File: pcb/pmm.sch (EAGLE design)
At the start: 25 parts, among them IC3 STM32F042F4, SW3 324_SW, SW4 324_SW, U2 USBC_16P, U4 XC6206_DEV

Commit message: fixed card edge connector footprint
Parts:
- JP1: device pinhead:PINHD-2X4 -> pmm:PINHEAD_PINHD-2X4
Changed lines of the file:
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@@
 <part name="R5" library="joyAnalog" deviceset="RESISTOR" device="0805-RES" value="10K"/>
 <part name="GND10" library="supply1" deviceset="GND" device=""/>
-<part name="JP1" library="pinhead" library_urn="urn:adsk.eagle:library:325" deviceset="PINHD-2X4" device="" package3d_urn="urn:adsk.eagle:package:22461/2"/>
+<part name="JP1" library="pmm" deviceset="PINHEAD_PINHD-2X4" device=""/>
 <part name="U4" library="3pos_slide_switch" deviceset="XC6206_DEV" device=""/>
 <part name="C2" library="clock" deviceset="CAP" device="0805" value="10uF"/>

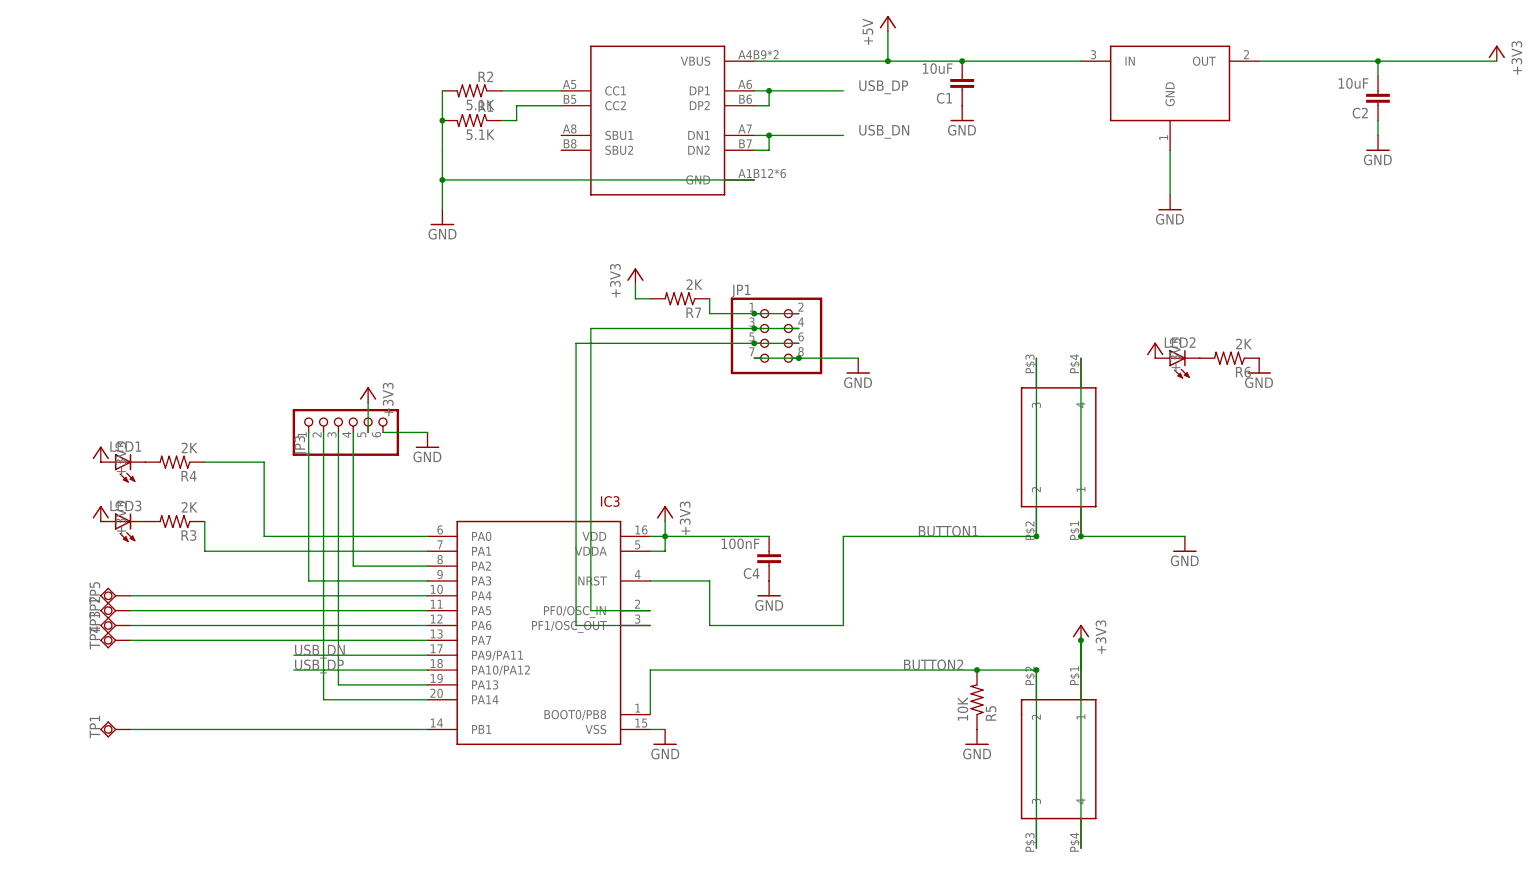
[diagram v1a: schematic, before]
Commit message: updated component values
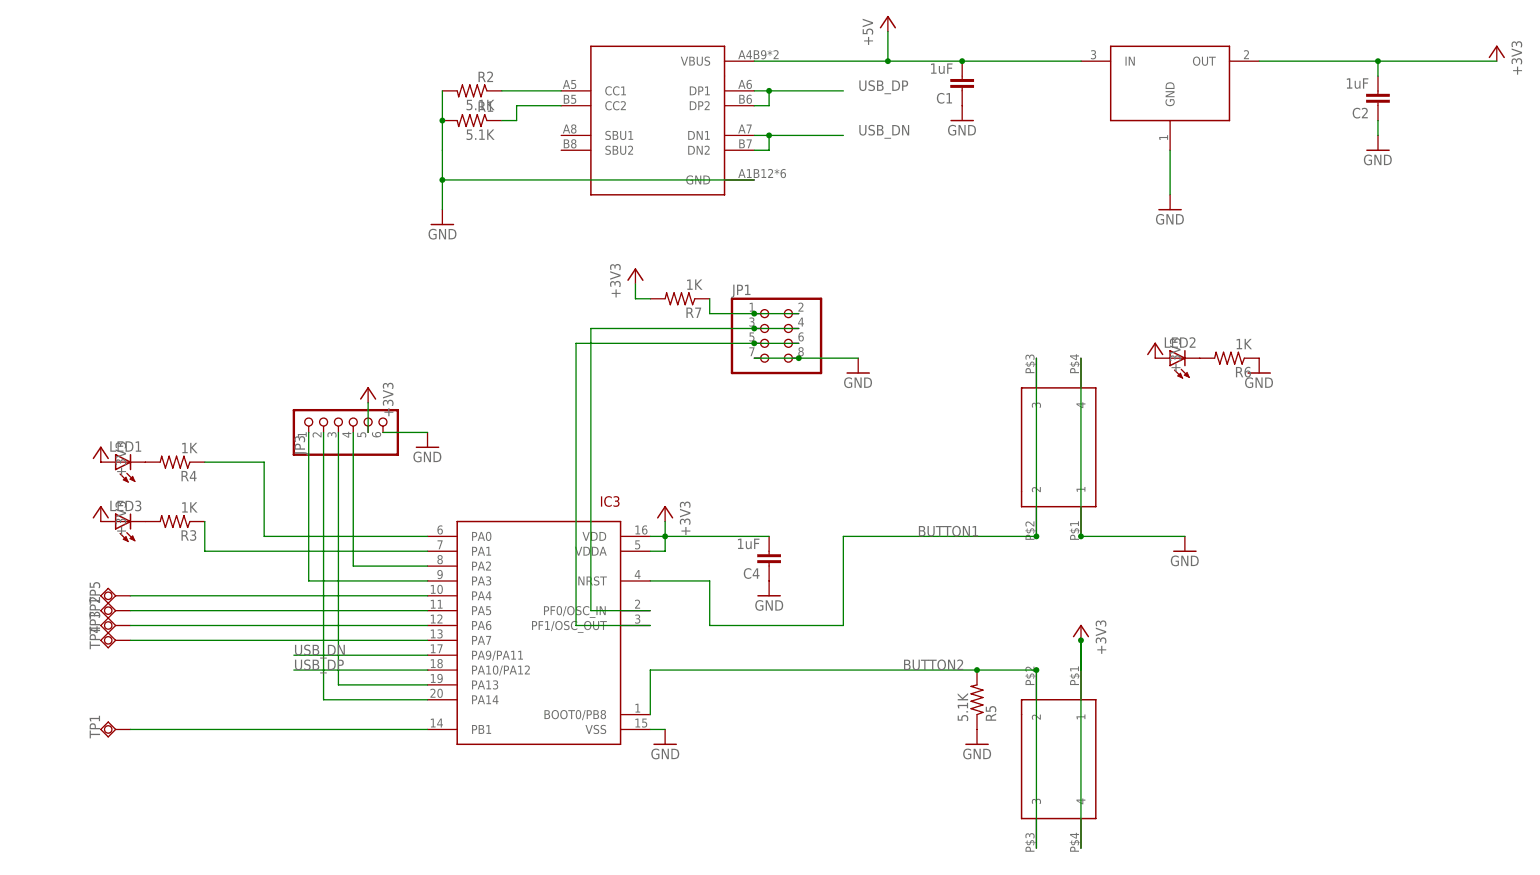
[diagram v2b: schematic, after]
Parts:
- C1, C2: value 10uF -> 1uF
- C4: value 100nF -> 1uF
- R3, R4, R6, R7: value 2K -> 1K
- R5: value 10K -> 5.1K
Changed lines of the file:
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@@
 <part name="R1" library="joyAnalog" deviceset="RESISTOR" device="0805-RES" value="5.1K"/>
 <part name="R2" library="joyAnalog" deviceset="RESISTOR" device="0805-RES" value="5.1K"/>
-<part name="C1" library="clock" deviceset="CAP" device="0805" value="10uF"/>
+<part name="C1" library="clock" deviceset="CAP" device="0805" value="1uF"/>
 <part name="GND16" library="supply1" library_urn="urn:adsk.eagle:library:371" deviceset="GND" device=""/>
 <part name="GND1" library="supply1" library_urn="urn:adsk.eagle:library:371" deviceset="GND" device=""/>
@@
 <part name="+3V1" library="supply1" library_urn="urn:adsk.eagle:library:371" deviceset="+3V3" device=""/>
 <part name="GND5" library="supply1" deviceset="GND" device=""/>
-<part name="C4" library="clock" deviceset="CAP" device="0805" value="100nF"/>
+<part name="C4" library="clock" deviceset="CAP" device="0805" value="1uF"/>
 <part name="GND8" library="supply1" deviceset="GND" device=""/>
 <part name="GND11" library="supply1" library_urn="urn:adsk.eagle:library:371" deviceset="GND" device=""/>
@@
 <part name="SW4" library="3pos_slide_switch_centered" deviceset="324_SW" device="" value="324_SW"/>
 <part name="LED1" library="adafruit" deviceset="LED" device="CHIP-LED0805"/>
-<part name="R4" library="SparkFun-Passives" deviceset="RESISTOR" device="0805-RES" value="2K"/>
+<part name="R4" library="SparkFun-Passives" deviceset="RESISTOR" device="0805-RES" value="1K"/>
 <part name="+3V9" library="backplane" deviceset="+3V3" device=""/>
 <part name="+3V16" library="backplane" deviceset="+3V3" device=""/>
 <part name="LED2" library="adafruit" deviceset="LED" device="CHIP-LED0805"/>
-<part name="R6" library="SparkFun-Passives" deviceset="RESISTOR" device="0805-RES" value="2K"/>
+<part name="R6" library="SparkFun-Passives" deviceset="RESISTOR" device="0805-RES" value="1K"/>
 <part name="GND9" library="backplane" deviceset="GND" device=""/>
 <part name="+3V2" library="supply1" library_urn="urn:adsk.eagle:library:371" deviceset="+3V3" device=""/>
-<part name="R5" library="joyAnalog" deviceset="RESISTOR" device="0805-RES" value="10K"/>
+<part name="R5" library="joyAnalog" deviceset="RESISTOR" device="0805-RES" value="5.1K"/>
 <part name="GND10" library="supply1" deviceset="GND" device=""/>
 <part name="JP1" library="pmm" deviceset="PINHEAD_PINHD-2X4" device=""/>
 <part name="U4" library="3pos_slide_switch" deviceset="XC6206_DEV" device=""/>
-<part name="C2" library="clock" deviceset="CAP" device="0805" value="10uF"/>
+<part name="C2" library="clock" deviceset="CAP" device="0805" value="1uF"/>
 <part name="GND2" library="backplane" deviceset="GND" device=""/>
 <part name="+3V3" library="backplane" deviceset="+3V3" device=""/>
 <part name="LED3" library="adafruit" deviceset="LED" device="CHIP-LED0805"/>
-<part name="R3" library="SparkFun-Passives" deviceset="RESISTOR" device="0805-RES" value="2K"/>
+<part name="R3" library="SparkFun-Passives" deviceset="RESISTOR" device="0805-RES" value="1K"/>
 <part name="+3V4" library="backplane" deviceset="+3V3" device=""/>
 <part name="JP3" library="pinhead" library_urn="urn:adsk.eagle:library:325" deviceset="PINHD-1X6" device="" package3d_urn="urn:adsk.eagle:package:22472/2"/>
 <part name="+3V6" library="supply1" library_urn="urn:adsk.eagle:library:371" deviceset="+3V3" device=""/>
 <part name="GND3" library="backplane" deviceset="GND" device=""/>
-<part name="R7" library="SparkFun-Passives" deviceset="RESISTOR" device="0805-RES" value="2K"/>
+<part name="R7" library="SparkFun-Passives" deviceset="RESISTOR" device="0805-RES" value="1K"/>
 <part name="TP1" library="testpad" library_urn="urn:adsk.eagle:library:385" deviceset="TPSQ" device="TP10SQ" package3d_urn="urn:adsk.eagle:package:27962/1" value="TPSQTP10SQ"/>
 <part name="TP2" library="testpad" library_urn="urn:adsk.eagle:library:385" deviceset="TPSQ" device="TP10SQ" package3d_urn="urn:adsk.eagle:package:27962/1" value="TPSQTP10SQ"/>

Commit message: updated pcb for next production run
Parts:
- removed SW3: 324_SW, 3pos_slide_switch_centered:324_SW
- removed TP1, TP2, TP3, TP4, TP5: TPSQTP10SQ, testpad:TPSQTP10SQ
- added JP2: (no value), pinhead:PINHD-2X3
- added U$1: PINHD1X2, adafruit_changed:PINHD1X2
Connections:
- removed net BUTTON1: IC3.NRST, SW3.2, SW3.3
- new net N$16: IC3.PA4, U$1.1
- net GND: now also JP2.1; no longer SW3.1, SW3.4
- net N$11: now also IC3.PA5, JP2.4; no longer IC3.PA7, TP4.TP
- net N$12: now also JP2.6; no longer TP3.TP
- net N$13: now also IC3.PA7, JP2.3; no longer IC3.PA5, TP2.TP
- net N$14: now also JP2.5; no longer TP1.TP
- net N$15: now also IC3.NRST, JP2.2; no longer IC3.PA4, TP5.TP
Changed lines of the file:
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@@
 <?xml version="1.0" encoding="utf-8"?>
 <!DOCTYPE eagle SYSTEM "eagle.dtd">
-<eagle version="9.6.1">
+<eagle version="9.6.2">
 <drawing>
 <settings>
@@
 <part name="GND8" library="supply1" deviceset="GND" device=""/>
 <part name="GND11" library="supply1" library_urn="urn:adsk.eagle:library:371" deviceset="GND" device=""/>
-<part name="SW3" library="3pos_slide_switch_centered" deviceset="324_SW" device="" value="324_SW"/>
 <part name="SW4" library="3pos_slide_switch_centered" deviceset="324_SW" device="" value="324_SW"/>
 <part name="LED1" library="adafruit" deviceset="LED" device="CHIP-LED0805"/>
@@
 <part name="GND3" library="backplane" deviceset="GND" device=""/>
 <part name="R7" library="SparkFun-Passives" deviceset="RESISTOR" device="0805-RES" value="1K"/>
-<part name="TP1" library="testpad" library_urn="urn:adsk.eagle:library:385" deviceset="TPSQ" device="TP10SQ" package3d_urn="urn:adsk.eagle:package:27962/1" value="TPSQTP10SQ"/>
-<part name="TP2" library="testpad" library_urn="urn:adsk.eagle:library:385" deviceset="TPSQ" device="TP10SQ" package3d_urn="urn:adsk.eagle:package:27962/1" value="TPSQTP10SQ"/>
-<part name="TP3" library="testpad" library_urn="urn:adsk.eagle:library:385" deviceset="TPSQ" device="TP10SQ" package3d_urn="urn:adsk.eagle:package:27962/1" value="TPSQTP10SQ"/>
-<part name="TP4" library="testpad" library_urn="urn:adsk.eagle:library:385" deviceset="TPSQ" device="TP10SQ" package3d_urn="urn:adsk.eagle:package:27962/1" value="TPSQTP10SQ"/>
-<part name="TP5" library="testpad" library_urn="urn:adsk.eagle:library:385" deviceset="TPSQ" device="TP10SQ" package3d_urn="urn:adsk.eagle:package:27962/1" value="TPSQTP10SQ"/>
+<part name="JP2" library="pinhead" library_urn="urn:adsk.eagle:library:325" deviceset="PINHD-2X3" device="" package3d_urn="urn:adsk.eagle:package:22462/2"/>
+<part name="U$1" library="adafruit_changed" deviceset="PINHD1X2" device=""/>
 </parts>
 <sheets>
@@
 <attribute name="VALUE" x="43.18" y="27.94" size="1.778" layer="96" rot="MR0"/>
 </instance>
-<instance part="GND11" gate="1" x="111.76" y="38.1" smashed="yes">
-<attribute name="VALUE" x="109.22" y="35.56" size="1.778" layer="96"/>
-</instance>
-<instance part="SW3" gate="G$1" x="91.44" y="55.88" smashed="yes" rot="R90"/>
+<instance part="GND11" gate="1" x="-86.36" y="-2.54" smashed="yes">
+<attribute name="VALUE" x="-88.9" y="-5.08" size="1.778" layer="96"/>
+</instance>
 <instance part="SW4" gate="G$1" x="91.44" y="2.54" smashed="yes" rot="MR270"/>
 <instance part="LED1" gate="G$1" x="-71.12" y="53.34" smashed="yes" rot="R90">
@@
 <attribute name="VALUE" x="29.21" y="84.582" size="1.778" layer="96" rot="R180"/>
 </instance>
-<instance part="TP1" gate="G$1" x="-71.12" y="7.62" smashed="yes" rot="R270">
-<attribute name="NAME" x="-75.565" y="10.16" size="1.778" layer="95" rot="R270"/>
-<attribute name="TP_SIGNAL_NAME" x="-72.39" y="5.08" size="1.778" layer="97" rot="R270"/>
-</instance>
-<instance part="TP2" gate="G$1" x="-71.12" y="27.94" smashed="yes" rot="R270">
-<attribute name="NAME" x="-75.565" y="30.48" size="1.778" layer="95" rot="R270"/>
-<attribute name="TP_SIGNAL_NAME" x="-72.39" y="25.4" size="1.778" layer="97" rot="R270"/>
-</instance>
-<instance part="TP3" gate="G$1" x="-71.12" y="25.4" smashed="yes" rot="R270">
-<attribute name="NAME" x="-75.565" y="27.94" size="1.778" layer="95" rot="R270"/>
-<attribute name="TP_SIGNAL_NAME" x="-72.39" y="22.86" size="1.778" layer="97" rot="R270"/>
-</instance>
-<instance part="TP4" gate="G$1" x="-71.12" y="22.86" smashed="yes" rot="R270">
-<attribute name="NAME" x="-75.565" y="25.4" size="1.778" layer="95" rot="R270"/>
-<attribute name="TP_SIGNAL_NAME" x="-72.39" y="20.32" size="1.778" layer="97" rot="R270"/>
-</instance>
-<instance part="TP5" gate="G$1" x="-71.12" y="30.48" smashed="yes" rot="R270">
-<attribute name="NAME" x="-75.565" y="33.02" size="1.778" layer="95" rot="R270"/>
-<attribute name="TP_SIGNAL_NAME" x="-72.39" y="27.94" size="1.778" layer="97" rot="R270"/>
+<instance part="JP2" gate="A" x="-68.58" y="-2.54" smashed="yes">
+<attribute name="NAME" x="-74.93" y="3.175" size="1.778" layer="95"/>
+<attribute name="VALUE" x="-74.93" y="-10.16" size="1.778" layer="96"/>
+</instance>
+<instance part="U$1" gate="1" x="-76.2" y="33.02" smashed="yes" rot="R180">
+<attribute name="NAME" x="-69.85" y="27.305" size="1.778" layer="95" rot="R180"/>
+<attribute name="VALUE" x="-69.85" y="38.1" size="1.778" layer="96" rot="R180"/>
 </instance>
 </instances>
@@
 </segment>
 <segment>
-<pinref part="GND11" gate="1" pin="GND"/>
-<pinref part="SW3" gate="G$1" pin="1"/>
-<wire x1="93.98" y1="40.64" x2="111.76" y2="40.64" width="0.1524" layer="91"/>
-<pinref part="SW3" gate="G$1" pin="4"/>
-<wire x1="93.98" y1="71.12" x2="93.98" y2="40.64" width="0.1524" layer="91"/>
-<junction x="93.98" y="40.64"/>
-</segment>
-<segment>
 <pinref part="R6" gate="G$1" pin="1"/>
 <pinref part="GND9" gate="1" pin="GND"/>
@@
 <pinref part="GND3" gate="1" pin="GND"/>
 <wire x1="-25.4" y1="58.42" x2="-17.78" y2="58.42" width="0.1524" layer="91"/>
+</segment>
+<segment>
+<pinref part="JP2" gate="A" pin="1"/>
+<pinref part="GND11" gate="1" pin="GND"/>
+<wire x1="-71.12" y1="0" x2="-86.36" y2="0" width="0.1524" layer="91"/>
 </segment>
 </net>
@@
 <junction x="60.96" y="121.92"/>
 <pinref part="U4" gate="G$1" pin="IN"/>
-</segment>
-</net>
-<net name="BUTTON1" class="0">
-<segment>
-<label x="66.04" y="40.64" size="1.778" layer="95"/>
-<pinref part="SW3" gate="G$1" pin="2"/>
-<wire x1="53.34" y1="40.64" x2="86.36" y2="40.64" width="0.1524" layer="91"/>
-<pinref part="SW3" gate="G$1" pin="3"/>
-<wire x1="86.36" y1="71.12" x2="86.36" y2="40.64" width="0.1524" layer="91"/>
-<junction x="86.36" y="40.64"/>
-<pinref part="IC3" gate="G$1" pin="NRST"/>
-<wire x1="20.32" y1="33.02" x2="30.48" y2="33.02" width="0.1524" layer="91"/>
-<wire x1="30.48" y1="33.02" x2="30.48" y2="25.4" width="0.1524" layer="91"/>
-<wire x1="30.48" y1="25.4" x2="53.34" y2="25.4" width="0.1524" layer="91"/>
-<wire x1="53.34" y1="25.4" x2="53.34" y2="40.64" width="0.1524" layer="91"/>
 </segment>
 </net>
@@
 <net name="N$11" class="0">
 <segment>
+<pinref part="IC3" gate="G$1" pin="PA5"/>
+<wire x1="-17.78" y1="27.94" x2="-55.88" y2="27.94" width="0.1524" layer="91"/>
+<wire x1="-55.88" y1="27.94" x2="-55.88" y2="-2.54" width="0.1524" layer="91"/>
+<pinref part="JP2" gate="A" pin="4"/>
+<wire x1="-55.88" y1="-2.54" x2="-63.5" y2="-2.54" width="0.1524" layer="91"/>
+</segment>
+</net>
+<net name="N$12" class="0">
+<segment>
+<pinref part="IC3" gate="G$1" pin="PA6"/>
+<wire x1="-17.78" y1="25.4" x2="-53.34" y2="25.4" width="0.1524" layer="91"/>
+<wire x1="-53.34" y1="25.4" x2="-53.34" y2="-5.08" width="0.1524" layer="91"/>
+<pinref part="JP2" gate="A" pin="6"/>
+<wire x1="-53.34" y1="-5.08" x2="-63.5" y2="-5.08" width="0.1524" layer="91"/>
+</segment>
+</net>
+<net name="N$13" class="0">
+<segment>
 <pinref part="IC3" gate="G$1" pin="PA7"/>
-<pinref part="TP4" gate="G$1" pin="TP"/>
-<wire x1="-17.78" y1="22.86" x2="-68.58" y2="22.86" width="0.1524" layer="91"/>
-</segment>
-</net>
-<net name="N$12" class="0">
-<segment>
-<pinref part="IC3" gate="G$1" pin="PA6"/>
-<pinref part="TP3" gate="G$1" pin="TP"/>
-<wire x1="-17.78" y1="25.4" x2="-68.58" y2="25.4" width="0.1524" layer="91"/>
-</segment>
-</net>
-<net name="N$13" class="0">
-<segment>
-<pinref part="IC3" gate="G$1" pin="PA5"/>
-<pinref part="TP2" gate="G$1" pin="TP"/>
-<wire x1="-17.78" y1="27.94" x2="-68.58" y2="27.94" width="0.1524" layer="91"/>
+<wire x1="-17.78" y1="22.86" x2="-78.74" y2="22.86" width="0.1524" layer="91"/>
+<wire x1="-78.74" y1="22.86" x2="-78.74" y2="-2.54" width="0.1524" layer="91"/>
+<pinref part="JP2" gate="A" pin="3"/>
+<wire x1="-78.74" y1="-2.54" x2="-71.12" y2="-2.54" width="0.1524" layer="91"/>
 </segment>
 </net>
@@
 <segment>
 <pinref part="IC3" gate="G$1" pin="PB1"/>
-<pinref part="TP1" gate="G$1" pin="TP"/>
-<wire x1="-68.58" y1="7.62" x2="-17.78" y2="7.62" width="0.1524" layer="91"/>
+<wire x1="-17.78" y1="7.62" x2="-17.78" y2="-15.24" width="0.1524" layer="91"/>
+<wire x1="-17.78" y1="-15.24" x2="-78.74" y2="-15.24" width="0.1524" layer="91"/>
+<wire x1="-78.74" y1="-15.24" x2="-78.74" y2="-5.08" width="0.1524" layer="91"/>
+<pinref part="JP2" gate="A" pin="5"/>
+<wire x1="-78.74" y1="-5.08" x2="-71.12" y2="-5.08" width="0.1524" layer="91"/>
 </segment>
 </net>
 <net name="N$15" class="0">
 <segment>
+<pinref part="IC3" gate="G$1" pin="NRST"/>
+<wire x1="20.32" y1="33.02" x2="33.02" y2="33.02" width="0.1524" layer="91"/>
+<wire x1="33.02" y1="33.02" x2="33.02" y2="0" width="0.1524" layer="91"/>
+<pinref part="JP2" gate="A" pin="2"/>
+<wire x1="33.02" y1="0" x2="-63.5" y2="0" width="0.1524" layer="91"/>
+</segment>
+</net>
+<net name="N$16" class="0">
+<segment>
 <pinref part="IC3" gate="G$1" pin="PA4"/>
-<pinref part="TP5" gate="G$1" pin="TP"/>
-<wire x1="-17.78" y1="30.48" x2="-68.58" y2="30.48" width="0.1524" layer="91"/>
-</segment>
-</net>
+<pinref part="U$1" gate="1" pin="1"/>
+<wire x1="-17.78" y1="30.48" x2="-73.66" y2="30.48" width="0.1524" layer="91"/>
+</segment>
+</net>

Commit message: cleanup
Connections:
- net GND: now also U$1.2
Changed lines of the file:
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@@
 <part name="JP2" library="pinhead" library_urn="urn:adsk.eagle:library:325" deviceset="PINHD-2X3" device="" package3d_urn="urn:adsk.eagle:package:22462/2"/>
 <part name="U$1" library="adafruit_changed" deviceset="PINHD1X2" device=""/>
+<part name="GND4" library="backplane" deviceset="GND" device=""/>
 </parts>
 <sheets>
@@
 <attribute name="NAME" x="-69.85" y="27.305" size="1.778" layer="95" rot="R180"/>
 <attribute name="VALUE" x="-69.85" y="38.1" size="1.778" layer="96" rot="R180"/>
+</instance>
+<instance part="GND4" gate="1" x="-86.36" y="30.48" smashed="yes">
+<attribute name="VALUE" x="-88.9" y="27.94" size="1.778" layer="96"/>
 </instance>
 </instances>
@@
 <wire x1="-71.12" y1="0" x2="-86.36" y2="0" width="0.1524" layer="91"/>
 </segment>
+<segment>
+<pinref part="U$1" gate="1" pin="2"/>
+<pinref part="GND4" gate="1" pin="GND"/>
+<wire x1="-73.66" y1="33.02" x2="-86.36" y2="33.02" width="0.1524" layer="91"/>
+</segment>
 </net>
